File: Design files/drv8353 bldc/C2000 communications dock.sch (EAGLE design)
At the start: 28 parts, among them IC1 ADUM1311ARWZ, J3 SS-6488-NF-A431, U1 3352T-1-203LF

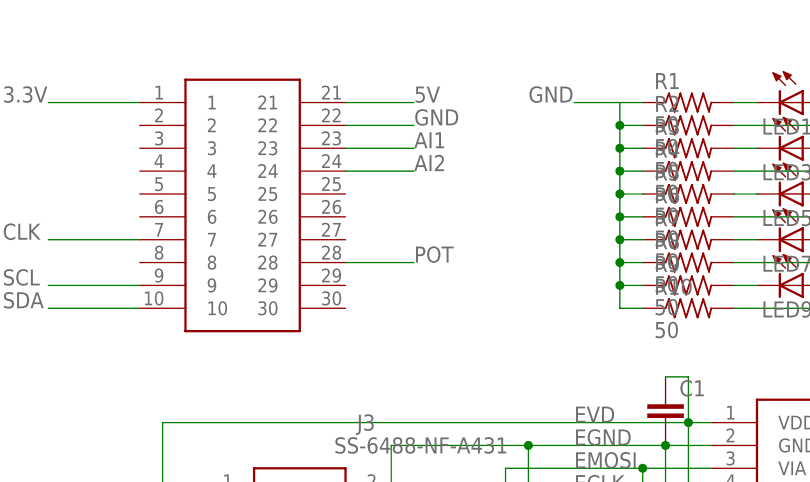
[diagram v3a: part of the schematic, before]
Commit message: moved analog signals top adc-b pins
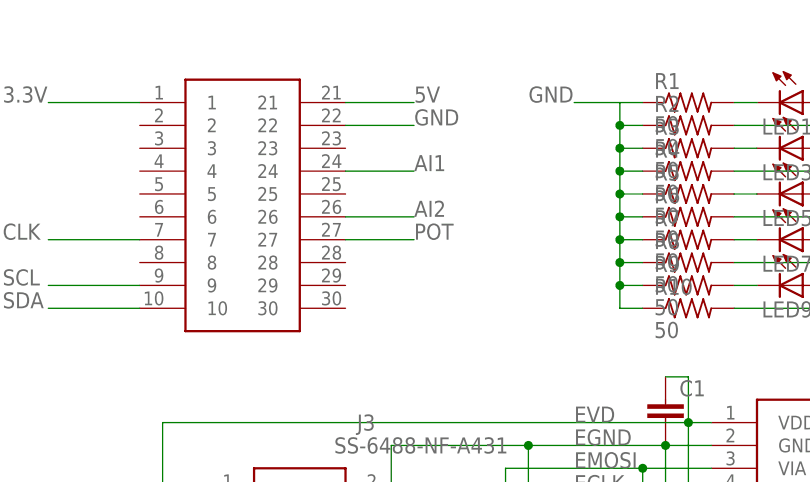
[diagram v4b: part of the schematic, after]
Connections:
- net AI1: now also U$1.24; no longer U$1.23
- net AI2: now also U$1.26; no longer U$1.24
- net POT: now also U$1.27; no longer U$1.28
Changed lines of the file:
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@@
 <net name="AI1" class="0">
-<segment>
-<pinref part="U$1" gate="G$1" pin="23"/>
-<wire x1="17.78" y1="55.88" x2="25.4" y2="55.88" width="0.1524" layer="91"/>
-<label x="25.4" y="55.88" size="1.778" layer="95"/>
-</segment>
 <segment>
 <pinref part="SV1" gate="G$1" pin="4"/>
@@
 <label x="149.86" y="12.7" size="1.778" layer="95"/>
 </segment>
-</net>
-<net name="AI2" class="0">
 <segment>
 <pinref part="U$1" gate="G$1" pin="24"/>
@@
 <label x="25.4" y="53.34" size="1.778" layer="95"/>
 </segment>
+</net>
+<net name="AI2" class="0">
 <segment>
 <pinref part="SV1" gate="G$1" pin="6"/>
 <wire x1="144.78" y1="15.24" x2="149.86" y2="15.24" width="0.1524" layer="91"/>
 <label x="149.86" y="15.24" size="1.778" layer="95"/>
+</segment>
+<segment>
+<pinref part="U$1" gate="G$1" pin="26"/>
+<wire x1="17.78" y1="48.26" x2="25.4" y2="48.26" width="0.1524" layer="91"/>
+<label x="25.4" y="48.26" size="1.778" layer="95"/>
 </segment>
 </net>
@@
 </segment>
 <segment>
-<pinref part="U$1" gate="G$1" pin="28"/>
-<wire x1="17.78" y1="43.18" x2="25.4" y2="43.18" width="0.1524" layer="91"/>
-<label x="25.4" y="43.18" size="1.778" layer="95"/>
+<pinref part="U$1" gate="G$1" pin="27"/>
+<wire x1="17.78" y1="45.72" x2="25.4" y2="45.72" width="0.1524" layer="91"/>
+<label x="25.4" y="45.72" size="1.778" layer="95"/>
 </segment>
 </net>

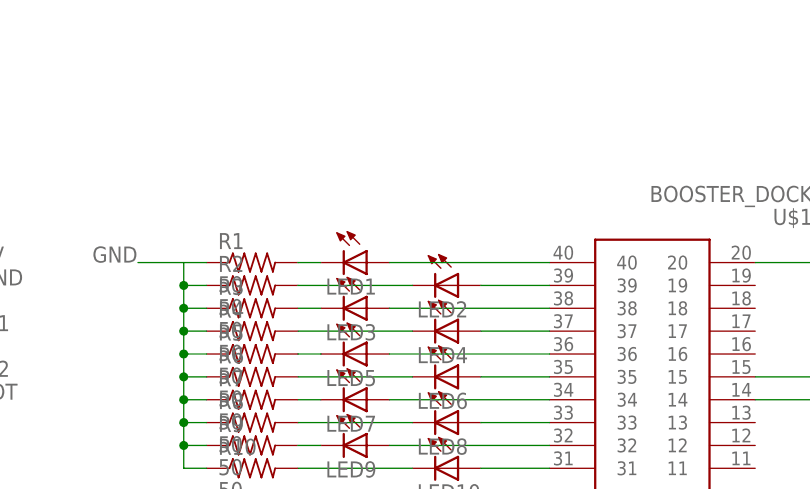
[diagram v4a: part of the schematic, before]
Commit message: adds enable link to comm board
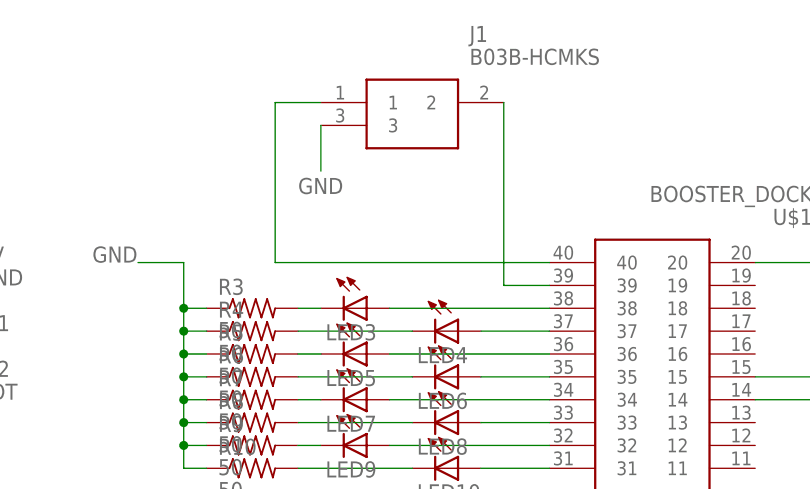
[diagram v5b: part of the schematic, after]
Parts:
- removed LED1, LED2: (no value), eagle-ltspice:LED_ESML0603
- removed R1, R2: 50, rcl:R-US_R0603
- added J1: B03B-HCMKS, AUX Lib:B03B-HCMKS
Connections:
- removed net N$17: LED1.C, R1.2
- removed net N$18: LED2.C, R2.2
- removed net N$3: LED2.A, U$1.39
- new net N$1: J1.1, U$1.40
- net GND: now also J1.3; no longer R1.1, R2.1
- net N$2: now also J1.2, U$1.39; no longer LED1.A, U$1.40
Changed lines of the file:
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@@
 <part name="J3" library="SamacSys_Parts" deviceset="SS-6488-NF-A431" device=""/>
 <part name="U$1" library="REV BLDC" deviceset="BOOSTER_DOCK" device=""/>
-<part name="LED1" library="eagle-ltspice" library_urn="urn:adsk.eagle:library:217" deviceset="LED_E" device="SML0603" package3d_urn="urn:adsk.eagle:package:13315/1"/>
-<part name="LED2" library="eagle-ltspice" library_urn="urn:adsk.eagle:library:217" deviceset="LED_E" device="SML0603" package3d_urn="urn:adsk.eagle:package:13315/1"/>
 <part name="LED3" library="eagle-ltspice" library_urn="urn:adsk.eagle:library:217" deviceset="LED_E" device="SML0603" package3d_urn="urn:adsk.eagle:package:13315/1"/>
 <part name="LED4" library="eagle-ltspice" library_urn="urn:adsk.eagle:library:217" deviceset="LED_E" device="SML0603" package3d_urn="urn:adsk.eagle:package:13315/1"/>
@@
 <part name="LED9" library="eagle-ltspice" library_urn="urn:adsk.eagle:library:217" deviceset="LED_E" device="SML0603" package3d_urn="urn:adsk.eagle:package:13315/1"/>
 <part name="LED10" library="eagle-ltspice" library_urn="urn:adsk.eagle:library:217" deviceset="LED_E" device="SML0603" package3d_urn="urn:adsk.eagle:package:13315/1"/>
-<part name="R1" library="rcl" library_urn="urn:adsk.eagle:library:334" deviceset="R-US_" device="R0603" package3d_urn="urn:adsk.eagle:package:23555/3" value="50"/>
-<part name="R2" library="rcl" library_urn="urn:adsk.eagle:library:334" deviceset="R-US_" device="R0603" package3d_urn="urn:adsk.eagle:package:23555/3" value="50"/>
 <part name="R3" library="rcl" library_urn="urn:adsk.eagle:library:334" deviceset="R-US_" device="R0603" package3d_urn="urn:adsk.eagle:package:23555/3" value="50"/>
 <part name="R4" library="rcl" library_urn="urn:adsk.eagle:library:334" deviceset="R-US_" device="R0603" package3d_urn="urn:adsk.eagle:package:23555/3" value="50"/>
@@
 <part name="C2" library="rcl" library_urn="urn:adsk.eagle:library:334" deviceset="C-EU" device="C0603" package3d_urn="urn:adsk.eagle:package:23616/2"/>
 <part name="SV2" library="con-lsta" library_urn="urn:adsk.eagle:library:161" deviceset="FE05-1" device="" package3d_urn="urn:adsk.eagle:package:8190/1"/>
+<part name="J1" library="AUX Lib" deviceset="B03B-HCMKS" device=""/>
 </parts>
 <sheets>
@@
 <attribute name="VALUE" x="118.11" y="68.58" size="1.778" layer="96" rot="R180" align="center-left"/>
 </instance>
-<instance part="LED1" gate="G$1" x="68.58" y="60.96" smashed="yes" rot="R270">
-<attribute name="NAME" x="64.008" y="57.404" size="1.778" layer="95"/>
-<attribute name="VALUE" x="64.008" y="55.245" size="1.778" layer="96"/>
-</instance>
-<instance part="LED2" gate="G$1" x="78.74" y="58.42" smashed="yes" rot="R270">
-<attribute name="NAME" x="74.168" y="54.864" size="1.778" layer="95"/>
-<attribute name="VALUE" x="74.168" y="52.705" size="1.778" layer="96"/>
-</instance>
 <instance part="LED3" gate="G$1" x="68.58" y="55.88" smashed="yes" rot="R270">
 <attribute name="NAME" x="64.008" y="52.324" size="1.778" layer="95"/>
@@
 <attribute name="VALUE" x="74.168" y="32.385" size="1.778" layer="96"/>
 </instance>
-<instance part="R1" gate="G$1" x="55.88" y="60.96" smashed="yes">
-<attribute name="NAME" x="52.07" y="62.4586" size="1.778" layer="95"/>
-<attribute name="VALUE" x="52.07" y="57.658" size="1.778" layer="96"/>
-</instance>
-<instance part="R2" gate="G$1" x="55.88" y="58.42" smashed="yes">
-<attribute name="NAME" x="52.07" y="59.9186" size="1.778" layer="95"/>
-<attribute name="VALUE" x="52.07" y="55.118" size="1.778" layer="96"/>
-</instance>
 <instance part="R3" gate="G$1" x="55.88" y="55.88" smashed="yes">
 <attribute name="NAME" x="52.07" y="57.3786" size="1.778" layer="95"/>
@@
 <attribute name="VALUE" x="60.96" y="-3.81" size="1.778" layer="96" rot="R90"/>
 <attribute name="NAME" x="42.418" y="-3.81" size="1.778" layer="95" rot="R90"/>
+</instance>
+<instance part="J1" gate="G$1" x="63.5" y="78.74" smashed="yes">
+<attribute name="NAME" x="80.01" y="86.36" size="1.778" layer="95" align="center-left"/>
+<attribute name="VALUE" x="80.01" y="83.82" size="1.778" layer="96" align="center-left"/>
 </instance>
 </instances>
@@
 <wire x1="48.26" y1="50.8" x2="48.26" y2="53.34" width="0.1524" layer="91"/>
 <wire x1="48.26" y1="53.34" x2="48.26" y2="55.88" width="0.1524" layer="91"/>
-<wire x1="48.26" y1="55.88" x2="48.26" y2="58.42" width="0.1524" layer="91"/>
-<wire x1="48.26" y1="58.42" x2="48.26" y2="60.96" width="0.1524" layer="91"/>
+<wire x1="48.26" y1="55.88" x2="48.26" y2="60.96" width="0.1524" layer="91"/>
 <wire x1="48.26" y1="60.96" x2="43.18" y2="60.96" width="0.1524" layer="91"/>
-<pinref part="R1" gate="G$1" pin="1"/>
-<wire x1="48.26" y1="60.96" x2="50.8" y2="60.96" width="0.1524" layer="91"/>
-<pinref part="R2" gate="G$1" pin="1"/>
-<wire x1="50.8" y1="58.42" x2="48.26" y2="58.42" width="0.1524" layer="91"/>
-<junction x="48.26" y="58.42"/>
 <pinref part="R3" gate="G$1" pin="1"/>
 <wire x1="50.8" y1="55.88" x2="48.26" y2="55.88" width="0.1524" layer="91"/>
@@
 <label x="116.84" y="17.78" size="1.778" layer="95"/>
 </segment>
+<segment>
+<pinref part="J1" gate="G$1" pin="3"/>
+<wire x1="63.5" y1="76.2" x2="63.5" y2="71.12" width="0.1524" layer="91"/>
+<label x="60.96" y="68.58" size="1.778" layer="95"/>
+</segment>
 </net>
 <net name="MISO" class="0">
@@
 </segment>
 </net>
-<net name="N$2" class="0">
-<segment>
-<pinref part="U$1" gate="G$1" pin="40"/>
-<pinref part="LED1" gate="G$1" pin="A"/>
-<wire x1="88.9" y1="60.96" x2="71.12" y2="60.96" width="0.1524" layer="91"/>
-</segment>
-</net>
-<net name="N$3" class="0">
-<segment>
-<pinref part="U$1" gate="G$1" pin="39"/>
-<pinref part="LED2" gate="G$1" pin="A"/>
-<wire x1="88.9" y1="58.42" x2="81.28" y2="58.42" width="0.1524" layer="91"/>
-</segment>
-</net>
 <net name="N$4" class="0">
 <segment>
@@
 </segment>
 </net>
-<net name="N$17" class="0">
-<segment>
-<pinref part="LED1" gate="G$1" pin="C"/>
-<pinref part="R1" gate="G$1" pin="2"/>
-<wire x1="63.5" y1="60.96" x2="60.96" y2="60.96" width="0.1524" layer="91"/>
-</segment>
-</net>
-<net name="N$18" class="0">
-<segment>
-<pinref part="LED2" gate="G$1" pin="C"/>
-<pinref part="R2" gate="G$1" pin="2"/>
-<wire x1="73.66" y1="58.42" x2="60.96" y2="58.42" width="0.1524" layer="91"/>
-</segment>
-</net>
 <net name="N$19" class="0">
 <segment>
@@
 </segment>
 </net>
+<net name="N$1" class="0">
+<segment>
+<pinref part="J1" gate="G$1" pin="1"/>
+<wire x1="63.5" y1="78.74" x2="58.42" y2="78.74" width="0.1524" layer="91"/>
+<wire x1="58.42" y1="78.74" x2="58.42" y2="60.96" width="0.1524" layer="91"/>
+<pinref part="U$1" gate="G$1" pin="40"/>
+<wire x1="58.42" y1="60.96" x2="88.9" y2="60.96" width="0.1524" layer="91"/>
+</segment>
+</net>
+<net name="N$2" class="0">
+<segment>
+<pinref part="J1" gate="G$1" pin="2"/>
+<wire x1="83.82" y1="78.74" x2="83.82" y2="58.42" width="0.1524" layer="91"/>
+<pinref part="U$1" gate="G$1" pin="39"/>
+<wire x1="83.82" y1="58.42" x2="88.9" y2="58.42" width="0.1524" layer="91"/>
+</segment>
+</net>

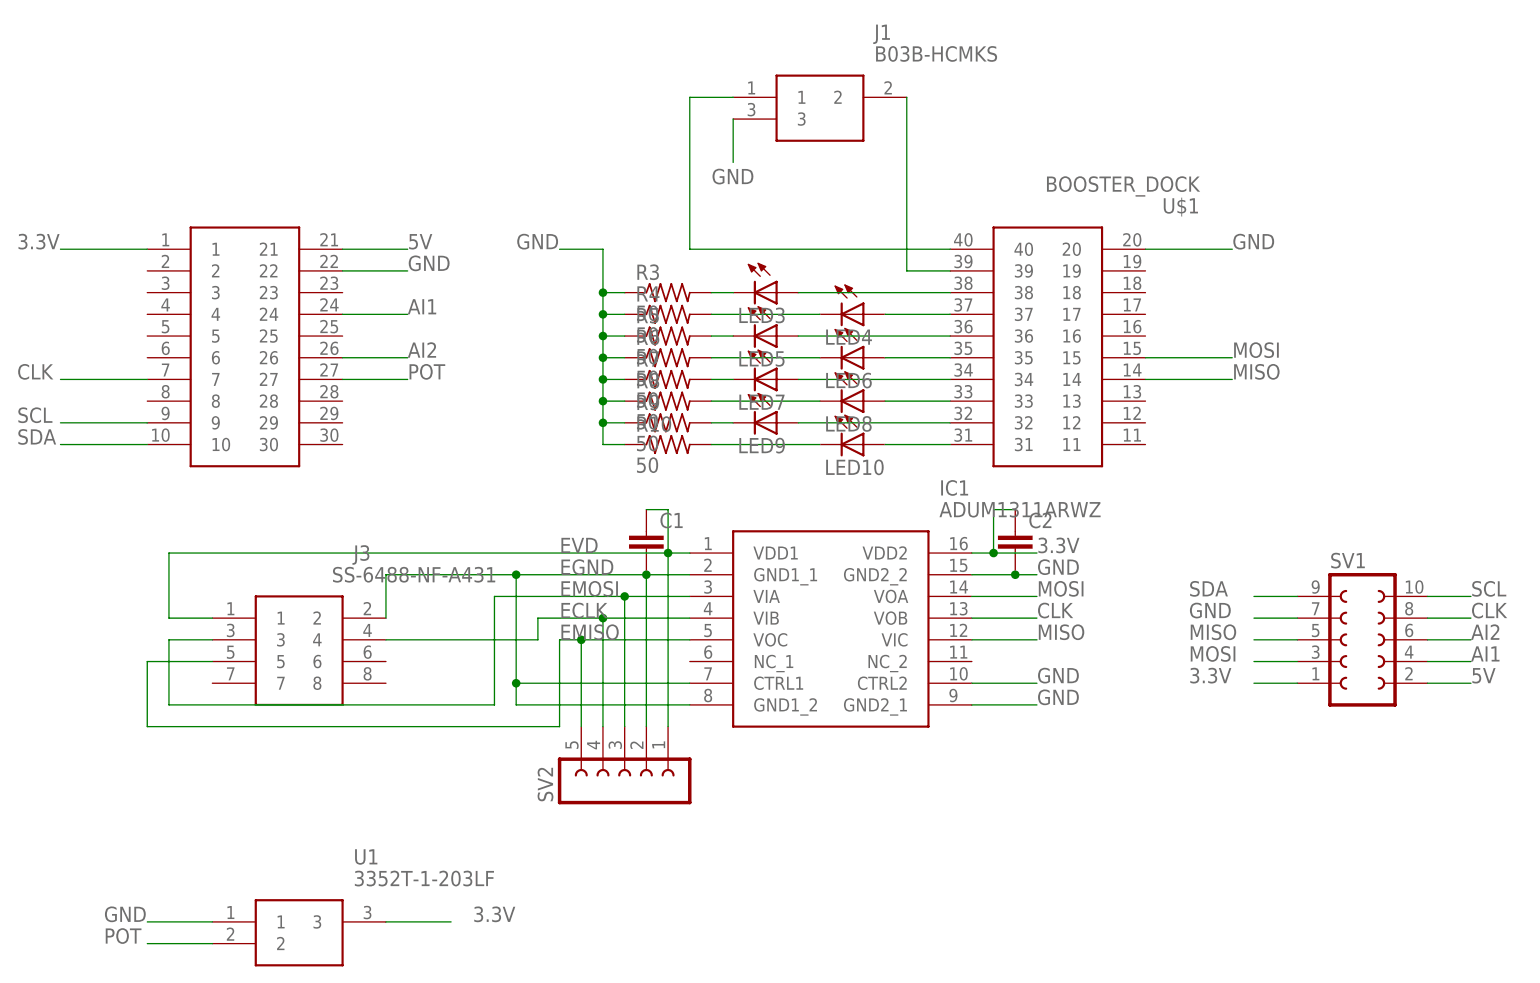
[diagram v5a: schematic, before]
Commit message: adds chip select to com board
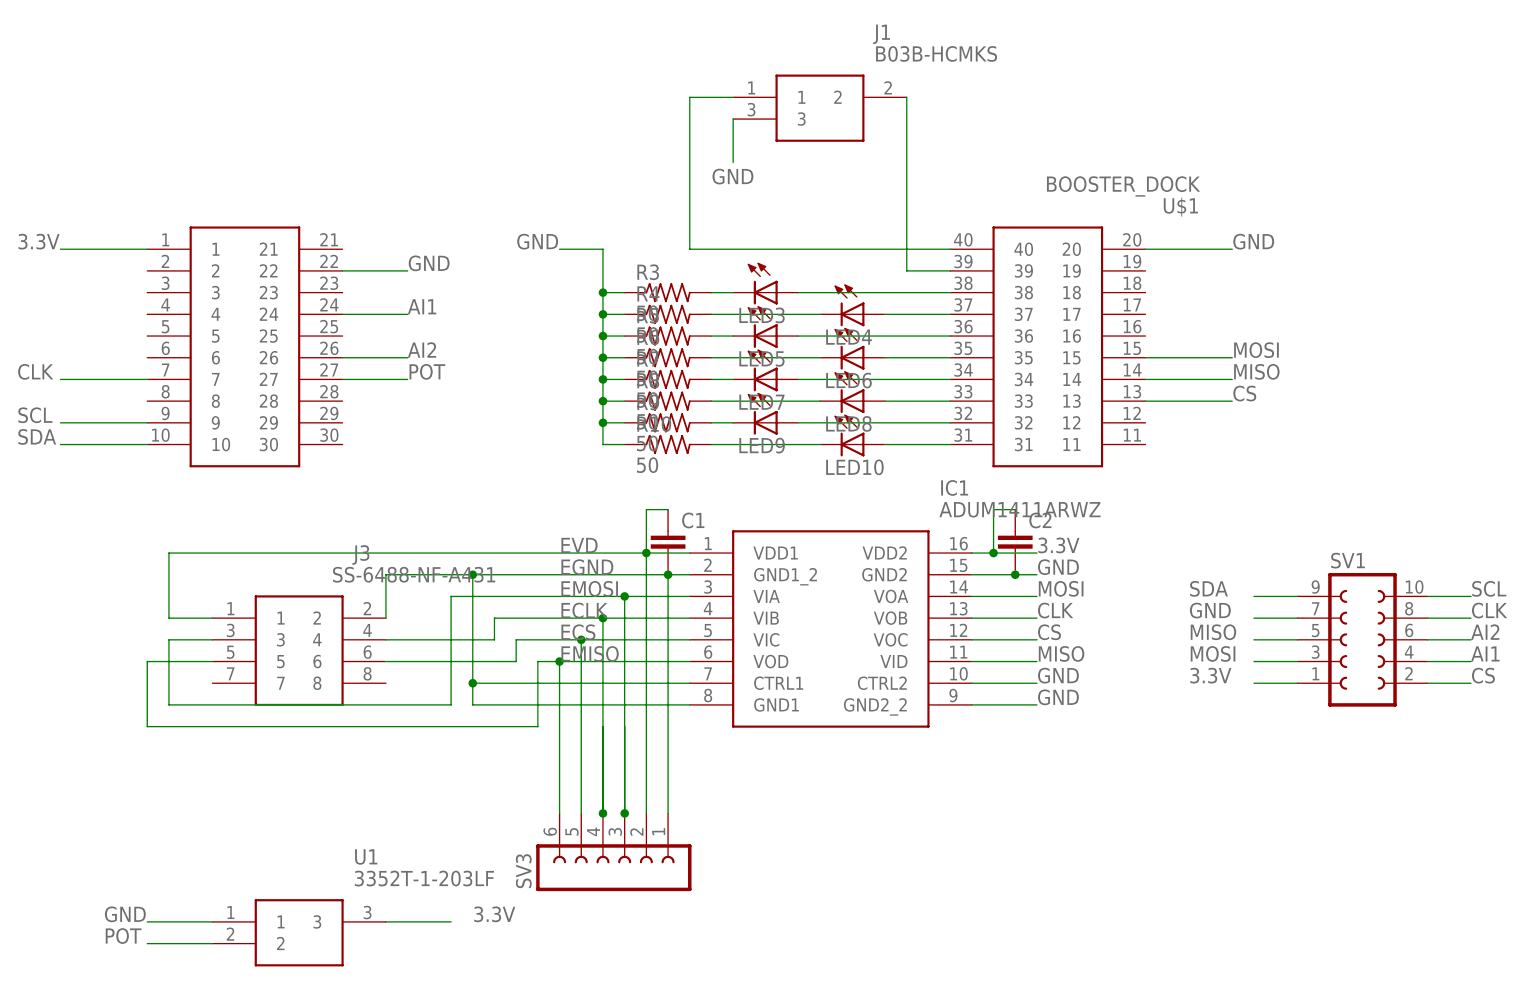
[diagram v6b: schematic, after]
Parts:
- removed SV2: (no value), con-lsta:FE05-1
- added SV3: (no value), con-lsta:FE06-1
- IC1: value ADUM1311ARWZ -> ADUM1411ARWZ; device SamacSys_Parts:ADUM1311ARWZ -> SamacSys_Parts:ADUM1411ARWZ
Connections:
- removed net 5V: SV1.2, U$1.21
- new net CS: IC1.VOC, SV1.2, U$1.13
- new net ECS: IC1.VIC, J3.6, SV3.5
- net ECLK: now also SV3.4; no longer SV2.4
- net EGND: now also IC1.GND1, SV3.1; no longer IC1.GND1_1, SV2.2
- net EMISO: now also IC1.VOD, SV3.6; no longer IC1.VOC, SV2.5
- net EMOSI: now also SV3.3; no longer SV2.3
- net EVD: now also SV3.2; no longer SV2.1
- net GND: now also IC1.GND2; no longer IC1.GND2_1
- net MISO: now also IC1.VID; no longer IC1.VIC
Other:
- moved on the sheet: C1
